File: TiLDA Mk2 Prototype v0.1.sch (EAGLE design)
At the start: 199 parts, among them IC1 ATSAM3X8EA-AU, IC10 MCP73831, IC2 MPU-6050, IC3 SRF-V1.2, IC5 S25FL216K0PMFI011, IC7 HMC5883LSMD (NP), IC8 MCP1825T-3302E/DC, IC9 TC1015-3V3, J1 ZX62-AB-5PA(11), J3 Arduino Headers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

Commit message: Parts: Miter corner board Prototype: Miter corner board
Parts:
- C101, C102, C103, C111, C133, C50: value SMC_B/10u/ -> 0805/10u/6V3/X5R
- C127, C135: value SMC_B/10u/ -> 0805/10u/6V3/X5R/(NP)
- C33, C36, C37: value 0805/22u/25V/X5R -> 0805/10u/6V3/X5R
- J6: value POWER-POD-EMF -> B016 - PowerPOD NCP1402 5V0
- J8: value (none) -> 1x02 RA Pin
- OUTLINE1: value TILDA_BOARDOUTLINE-VERYWIDE -> TILDA_BOARDOUTLINE-MITER; device TiLDA Mk2 Parts:TILDA_BOARDOUTLINE-VERYWIDE -> TiLDA Mk2 Parts:TILDA_BOARDOUTLINE-MITER
- renumbered U1 to J6
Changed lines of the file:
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@@
 <parts>
 <part name="FRAME1" library="TiLDA Mk2 Parts" deviceset="A3L-LOC" device=""/>
-<part name="OUTLINE1" library="TiLDA Mk2 Parts" deviceset="TILDA_BOARDOUTLINE" device="-VERYWIDE"/>
+<part name="OUTLINE1" library="TiLDA Mk2 Parts" deviceset="TILDA_BOARDOUTLINE" device="-MITER"/>
 <part name="LOGO1" library="TiLDA Mk2 Parts" deviceset="OSHW-LOGO" device="M"/>
 <part name="FID1" library="TiLDA Mk2 Parts" deviceset="FIDUCIAL" device="1X2.5-STOP"/>
@@
 <part name="GND17" library="TiLDA Mk2 Parts" deviceset="GND" device=""/>
 <part name="GND20" library="TiLDA Mk2 Parts" deviceset="GND" device=""/>
-<part name="C133" library="TiLDA Mk2 Parts" deviceset="CPOL-EU" device="-C0805RNDPOL" value="SMC_B/10u/"/>
+<part name="C133" library="TiLDA Mk2 Parts" deviceset="CPOL-EU" device="-C0805RNDPOL" value="0805/10u/6V3/X5R"/>
 <part name="C132" library="TiLDA Mk2 Parts" deviceset="C-EU" device="C0402-ARDUINO-ROUND" value="0402/100n/10V/X5R"/>
 <part name="GND22" library="TiLDA Mk2 Parts" deviceset="GND" device=""/>
@@
 <part name="L101" library="TiLDA Mk2 Parts" deviceset="WE-CBF" device="_0805" value="MH2029-300Y"/>
 <part name="L102" library="TiLDA Mk2 Parts" deviceset="WE-CBF" device="_0805" value="MH2029-300Y"/>
-<part name="C101" library="TiLDA Mk2 Parts" deviceset="CPOL-EU" device="-C0805RNDPOL" value="SMC_B/10u/"/>
-<part name="C111" library="TiLDA Mk2 Parts" deviceset="CPOL-EU" device="-C0805RNDPOL" value="SMC_B/10u/"/>
-<part name="C102" library="TiLDA Mk2 Parts" deviceset="CPOL-EU" device="-C0805RNDPOL" value="SMC_B/10u/"/>
-<part name="C103" library="TiLDA Mk2 Parts" deviceset="CPOL-EU" device="-C0805RNDPOL" value="SMC_B/10u/"/>
+<part name="C101" library="TiLDA Mk2 Parts" deviceset="CPOL-EU" device="-C0805RNDPOL" value="0805/10u/6V3/X5R"/>
+<part name="C111" library="TiLDA Mk2 Parts" deviceset="CPOL-EU" device="-C0805RNDPOL" value="0805/10u/6V3/X5R"/>
+<part name="C102" library="TiLDA Mk2 Parts" deviceset="CPOL-EU" device="-C0805RNDPOL" value="0805/10u/6V3/X5R"/>
+<part name="C103" library="TiLDA Mk2 Parts" deviceset="CPOL-EU" device="-C0805RNDPOL" value="0805/10u/6V3/X5R"/>
 <part name="L105" library="TiLDA Mk2 Parts" deviceset="WE-CBF" device="_0805" value="MH2029-300Y"/>
 <part name="R108" library="TiLDA Mk2 Parts" deviceset="R-EU_" device="R0402-ARDUINO-ROUND" value="0402/0R/5%/(NP)"/>
@@
 <part name="GND50" library="supply1" deviceset="GND" device=""/>
 <part name="C126" library="TiLDA Mk2 Parts" deviceset="C-EU" device="C0402-ARDUINO-ROUND" value="0402/10n/10V/Y5V"/>
-<part name="C127" library="TiLDA Mk2 Parts" deviceset="CPOL-EU" device="-C0805RNDPOL" value="SMC_B/10u/"/>
-<part name="C135" library="TiLDA Mk2 Parts" deviceset="CPOL-EU" device="-C0805RNDPOL" value="SMC_B/10u/"/>
+<part name="C127" library="TiLDA Mk2 Parts" deviceset="CPOL-EU" device="-C0805RNDPOL" value="0805/10u/6V3/X5R/(NP)"/>
+<part name="C135" library="TiLDA Mk2 Parts" deviceset="CPOL-EU" device="-C0805RNDPOL" value="0805/10u/6V3/X5R/(NP)"/>
 <part name="GND52" library="TiLDA Mk2 Parts" deviceset="GND" device=""/>
 <part name="R102" library="TiLDA Mk2 Parts" deviceset="R-EU_" device="R0402-ARDUINO-ROUND" value="0402/10K/5%"/>
 <part name="GND53" library="TiLDA Mk2 Parts" deviceset="GND" device=""/>
 <part name="R25" library="TiLDA Mk2 Parts" deviceset="R-EU_" device="R0402-ARDUINO-ROUND" value="0402/1K/5%"/>
-<part name="C36" library="TiLDA Mk2 Parts" deviceset="C-EU" device="C0805RND" value="0805/22u/25V/X5R"/>
+<part name="C36" library="TiLDA Mk2 Parts" deviceset="C-EU" device="C0805RND" value="0805/10u/6V3/X5R"/>
 <part name="C34" library="TiLDA Mk2 Parts" deviceset="C-EU" device="C0603-ROUND" value="0603/1u/10V/X5R"/>
 <part name="GND63" library="TiLDA Mk2 Parts" deviceset="GND" device=""/>
 <part name="GND64" library="TiLDA Mk2 Parts" deviceset="GND" device=""/>
-<part name="C33" library="TiLDA Mk2 Parts" deviceset="C-EU" device="C0805RND" value="0805/22u/25V/X5R"/>
+<part name="C33" library="TiLDA Mk2 Parts" deviceset="C-EU" device="C0805RND" value="0805/10u/6V3/X5R"/>
 <part name="GND65" library="TiLDA Mk2 Parts" deviceset="GND" device=""/>
 <part name="IC8" library="TiLDA Mk2 Parts" deviceset="MCP1825T-3302E/DC" device=""/>
@@
 <part name="H1" library="TiLDA Mk2 Parts" deviceset="MOUNT-HOLE" device="4.5-LWK" value=""/>
 <part name="H2" library="TiLDA Mk2 Parts" deviceset="MOUNT-HOLE" device="4.5-LWK" value=""/>
-<part name="C37" library="TiLDA Mk2 Parts" deviceset="C-EU" device="C0805RND" value="0805/22u/25V/X5R"/>
+<part name="C37" library="TiLDA Mk2 Parts" deviceset="C-EU" device="C0805RND" value="0805/10u/6V3/X5R"/>
 <part name="GND58" library="TiLDA Mk2 Parts" deviceset="GND" device=""/>
 <part name="C38" library="TiLDA Mk2 Parts" deviceset="C-EU" device="C0603-ROUND" value="0603/1u/10V/X5R"/>
@@
 <part name="R49" library="TiLDA Mk2 Parts" deviceset="R-EU_" device="R0402-ARDUINO-ROUND" value="0402/10K/5%"/>
 <part name="U2" library="TiLDA Mk2 Parts" deviceset="JHD12864-G13BSW-OUTLINE" device=""/>
-<part name="J8" library="TiLDA Mk2 Parts" deviceset="M02" device="RA"/>
+<part name="J8" library="TiLDA Mk2 Parts" deviceset="M02" device="RA" value="1x02 RA Pin"/>
 <part name="J7" library="TiLDA Mk2 Parts" deviceset="JHD12863-G13BSW-CONNECTOR" device="-SFV30R-2STE1HLF" value="SFV30R-2STE1HLF"/>
 <part name="C39" library="TiLDA Mk2 Parts" deviceset="C-EU" device="C0603-ROUND" value="0603/1u/10V/X5R"/>
@@
 <attribute name="TP_SIGNAL_NAME" value=""/>
 </part>
-<part name="U1" library="TiLDA Mk2 Parts" deviceset="POWER-POD" device="-EMF"/>
+<part name="J6" library="TiLDA Mk2 Parts" deviceset="POWER-POD" device="-EMF" value="B016 - PowerPOD NCP1402 5V0"/>
 <part name="R47" library="TiLDA Mk2 Parts" deviceset="R-EU_" device="R0402-ARDUINO-ROUND" value="0402/10K/5%"/>
 <part name="R48" library="TiLDA Mk2 Parts" deviceset="R-EU_" device="R0402-ARDUINO-ROUND" value="0402/10K/5%"/>
-<part name="C50" library="TiLDA Mk2 Parts" deviceset="CPOL-EU" device="-C0805RNDPOL" value="SMC_B/10u/"/>
+<part name="C50" library="TiLDA Mk2 Parts" deviceset="CPOL-EU" device="-C0805RNDPOL" value="0805/10u/6V3/X5R"/>
 <part name="GND9" library="TiLDA Mk2 Parts" deviceset="GND" device=""/>
 </parts>
@@
 <instance part="TP25" gate="G$1" x="673.1" y="83.82" rot="R270"/>
 <instance part="TP26" gate="G$1" x="670.56" y="182.88" rot="R270"/>
-<instance part="U1" gate="G$1" x="88.9" y="144.78"/>
+<instance part="J6" gate="G$1" x="88.9" y="144.78"/>
 <instance part="R47" gate="G$1" x="127" y="139.7" smashed="yes" rot="R90">
 <attribute name="NAME" x="128.27" y="143.7386" size="1.778" layer="95"/>
@@
 <wire x1="78.74" y1="147.32" x2="76.2" y2="147.32" width="0.1524" layer="91"/>
 <label x="76.2" y="147.32" size="1.778" layer="95" rot="MR0"/>
-<pinref part="U1" gate="G$1" pin="GND"/>
+<pinref part="J6" gate="G$1" pin="GND"/>
 </segment>
 <segment>
@@
 <wire x1="78.74" y1="149.86" x2="76.2" y2="149.86" width="0.1524" layer="91"/>
 <label x="76.2" y="149.86" size="1.778" layer="95" rot="MR0"/>
-<pinref part="U1" gate="G$1" pin="VIN"/>
+<pinref part="J6" gate="G$1" pin="VIN"/>
 </segment>
 <segment>
@@
 <wire x1="78.74" y1="144.78" x2="76.2" y2="144.78" width="0.1524" layer="91"/>
 <label x="76.2" y="144.78" size="1.778" layer="95" rot="MR0"/>
-<pinref part="U1" gate="G$1" pin="VOUT"/>
-</segment>
-</net>
+<pinref part="J6" gate="G$1" pin="VOUT"/>
+</segment>
+</net>

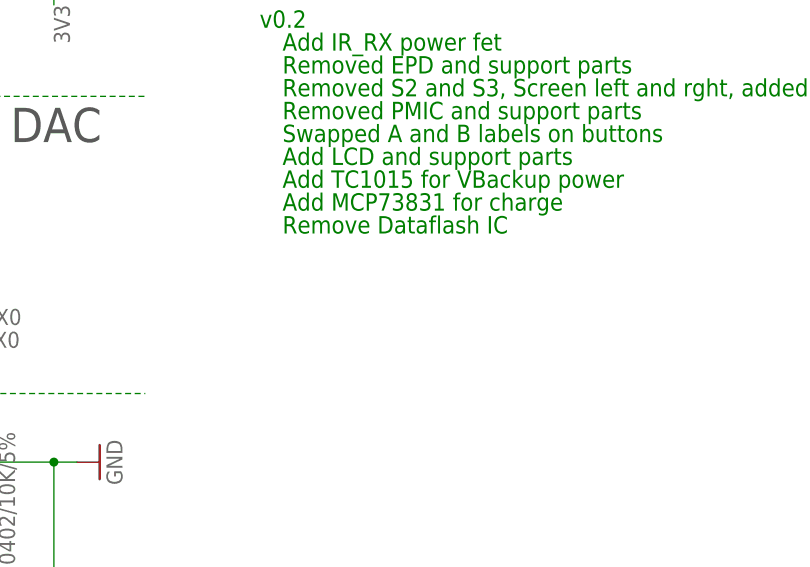
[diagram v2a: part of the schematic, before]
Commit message: Prototype: Slik screen updates
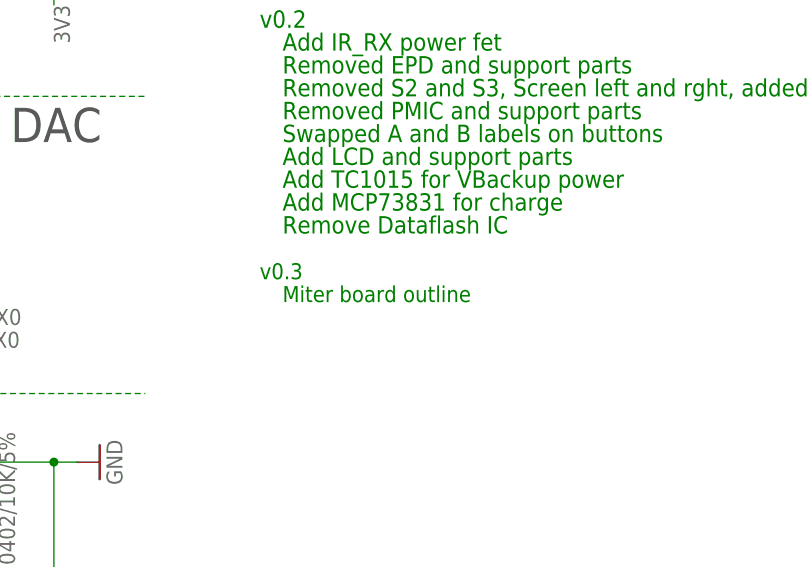
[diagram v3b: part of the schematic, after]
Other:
- note added: "Miter board outline"
- note added: "v0.3"
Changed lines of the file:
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@@
 <text x="474.98" y="2.54" size="1.9304" layer="91" rot="R90">VDDIO</text>
 <text x="487.68" y="2.54" size="1.9304" layer="91" rot="R90">VDDIO</text>
+<text x="795.02" y="147.32" size="1.778" layer="91">v0.3</text>
+<text x="797.56" y="144.78" size="1.778" layer="91">Miter board outline</text>
 </plain>
 <instances>

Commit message: Prototype: fixed LCD conections
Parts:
- Q12: value BSS84W -> 2N7002KW; device TiLDA Mk2 Parts:MOSFET-P-SC70-3 -> TiLDA Mk2 Parts:MOSFET-NSC70-3
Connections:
- removed net LCD_A: R45.1, U2.A
- new net N$1: R45.1, U2.K
- net 3V3: now also U2.A; no longer Q12.S, R43.2
- net GND: now also Q12.S, R43.2; no longer U2.K
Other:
- moved on the sheet: R45
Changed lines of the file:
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@@
 <attribute name="TP_SIGNAL_NAME" value=""/>
 </part>
-<part name="Q12" library="TiLDA Mk2 Parts" deviceset="MOSFET-P" device="-SC70-3" value="BSS84W"/>
 <part name="TP22" library="TiLDA Mk2 Parts" deviceset="TP" device="B1,27" value="PC12">
 <attribute name="TP_SIGNAL_NAME" value=""/>
@@
 <part name="C50" library="TiLDA Mk2 Parts" deviceset="CPOL-EU" device="-C0805RNDPOL" value="0805/10u/6V3/X5R"/>
 <part name="GND9" library="TiLDA Mk2 Parts" deviceset="GND" device=""/>
+<part name="Q12" library="TiLDA Mk2 Parts" deviceset="MOSFET-N" device="SC70-3" value="2N7002KW"/>
 </parts>
 <sheets>
@@
 <instance part="C46" gate="G$1" x="342.9" y="172.72" rot="R180"/>
 <instance part="C47" gate="G$1" x="347.98" y="172.72" rot="R180"/>
-<instance part="R45" gate="G$1" x="38.1" y="218.44"/>
+<instance part="R45" gate="G$1" x="40.64" y="218.44"/>
 <instance part="Q11" gate="G$1" x="264.16" y="162.56"/>
 <instance part="R43" gate="G$1" x="71.12" y="226.06"/>
@@
 </instance>
 <instance part="R46" gate="G$1" x="76.2" y="93.98" rot="R270"/>
-<instance part="GND1" gate="1" x="33.02" y="228.6" rot="R90"/>
+<instance part="GND1" gate="1" x="88.9" y="213.36"/>
 <instance part="GND2" gate="1" x="297.18" y="208.28" rot="R270"/>
 <instance part="GND3" gate="1" x="355.6" y="170.18"/>
@@
 <instance part="TP20" gate="G$1" x="683.26" y="172.72" rot="R270"/>
 <instance part="TP21" gate="G$1" x="673.1" y="119.38" rot="R270"/>
-<instance part="Q12" gate="G$1" x="60.96" y="218.44" rot="R270"/>
 <instance part="TP22" gate="G$1" x="675.64" y="106.68" rot="R270"/>
 <instance part="TP24" gate="G$1" x="584.2" y="40.64" rot="R180"/>
@@
 </instance>
 <instance part="GND9" gate="1" x="91.44" y="38.1"/>
+<instance part="Q12" gate="G$1" x="60.96" y="220.98" rot="MR270"/>
 </instances>
 <busses>
@@
 </segment>
 <segment>
-<pinref part="U2" gate="OUTLINE" pin="K"/>
-<wire x1="27.94" y1="228.6" x2="30.48" y2="228.6" width="0.1524" layer="91"/>
-<pinref part="GND1" gate="1" pin="GND"/>
-</segment>
-<segment>
 <pinref part="C50" gate="G$1" pin="-"/>
 <pinref part="GND9" gate="1" pin="GND"/>
 <wire x1="91.44" y1="40.64" x2="91.44" y2="43.18" width="0.1524" layer="91"/>
 </segment>
+<segment>
+<wire x1="88.9" y1="215.9" x2="88.9" y2="218.44" width="0.1524" layer="91"/>
+<pinref part="R43" gate="G$1" pin="2"/>
+<wire x1="88.9" y1="218.44" x2="66.04" y2="218.44" width="0.1524" layer="91"/>
+<wire x1="76.2" y1="226.06" x2="88.9" y2="226.06" width="0.1524" layer="91"/>
+<wire x1="88.9" y1="226.06" x2="88.9" y2="218.44" width="0.1524" layer="91"/>
+<junction x="88.9" y="218.44"/>
+<pinref part="GND1" gate="1" pin="GND"/>
+<pinref part="Q12" gate="G$1" pin="S"/>
+</segment>
 </net>
 <net name="PD10" class="0">
@@
 </segment>
 <segment>
-<wire x1="91.44" y1="218.44" x2="88.9" y2="218.44" width="0.1524" layer="91"/>
-<label x="91.44" y="218.44" size="1.778" layer="95"/>
-<pinref part="Q12" gate="G$1" pin="S"/>
-<pinref part="R43" gate="G$1" pin="2"/>
-<wire x1="88.9" y1="218.44" x2="66.04" y2="218.44" width="0.1524" layer="91"/>
-<wire x1="76.2" y1="226.06" x2="88.9" y2="226.06" width="0.1524" layer="91"/>
-<wire x1="88.9" y1="226.06" x2="88.9" y2="218.44" width="0.1524" layer="91"/>
-<junction x="88.9" y="218.44"/>
-</segment>
-<segment>
 <pinref part="Q11" gate="G$1" pin="S"/>
 <wire x1="264.16" y1="190.5" x2="264.16" y2="187.96" width="0.1524" layer="91"/>
@@
 <label x="561.34" y="226.06" size="1.9304" layer="95" rot="MR90"/>
 </segment>
+<segment>
+<pinref part="U2" gate="OUTLINE" pin="A"/>
+<wire x1="30.48" y1="228.6" x2="27.94" y2="228.6" width="0.1524" layer="91"/>
+<label x="30.48" y="228.6" size="1.778" layer="95"/>
+</segment>
 </net>
 <net name="LCD_POWER" class="0">
@@
 <label x="63.5" y="228.6" size="1.778" layer="95" rot="R90"/>
 <wire x1="63.5" y1="223.52" x2="63.5" y2="226.06" width="0.1524" layer="91"/>
-<pinref part="Q12" gate="G$1" pin="G"/>
 <pinref part="R43" gate="G$1" pin="1"/>
 <wire x1="63.5" y1="226.06" x2="63.5" y2="228.6" width="0.1524" layer="91"/>
 <wire x1="66.04" y1="226.06" x2="63.5" y2="226.06" width="0.1524" layer="91"/>
 <junction x="63.5" y="226.06"/>
+<pinref part="Q12" gate="G$1" pin="G"/>
 </segment>
 <segment>
@@
 </segment>
 </net>
-<net name="LCD_A" class="0">
-<segment>
-<pinref part="R45" gate="G$1" pin="1"/>
-<pinref part="U2" gate="OUTLINE" pin="A"/>
-<wire x1="33.02" y1="218.44" x2="27.94" y2="218.44" width="0.1524" layer="91"/>
-</segment>
-</net>
 <net name="LCD_V1" class="0">
 <segment>
@@
 <segment>
 <pinref part="R45" gate="G$1" pin="2"/>
+<wire x1="55.88" y1="218.44" x2="45.72" y2="218.44" width="0.1524" layer="91"/>
 <pinref part="Q12" gate="G$1" pin="D"/>
-<wire x1="55.88" y1="218.44" x2="43.18" y2="218.44" width="0.1524" layer="91"/>
 </segment>
 </net>
@@
 </segment>
 </net>
+<net name="N$1" class="0">
+<segment>
+<pinref part="U2" gate="OUTLINE" pin="K"/>
+<pinref part="R45" gate="G$1" pin="1"/>
+<wire x1="27.94" y1="218.44" x2="35.56" y2="218.44" width="0.1524" layer="91"/>
+</segment>
+</net>

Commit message: Prototype: more curves
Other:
- note added: "Off"
- note added: "On"
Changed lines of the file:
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@@
 <text x="795.02" y="147.32" size="1.778" layer="91">v0.3</text>
 <text x="797.56" y="144.78" size="1.778" layer="91">Miter board outline</text>
+<text x="88.9" y="7.62" size="1.778" layer="91">On</text>
+<text x="88.9" y="17.78" size="1.778" layer="91">Off</text>
 </plain>
 <instances>

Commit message: Prototype: Allow power from just USB
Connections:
- removed net 4V2: S8.O
- net VBUS: now also S8.O
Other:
- note added: "Allow power from USB"
- note added: "Battery is charged in both cases"
- note added: "Curve all the tracks"
- note added: "Off posotion power is taken from USB"
- note added: "Off/USB"
- note added: "On posotion power is taken from the battery"
- note added: "On/Battery"
- note added: "Silk screen updates"
- note added: "v0.333333333333333333"
- note removed: "Off"
- note removed: "On"
- note removed: "v0.3"
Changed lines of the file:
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@@
 <text x="474.98" y="2.54" size="1.9304" layer="91" rot="R90">VDDIO</text>
 <text x="487.68" y="2.54" size="1.9304" layer="91" rot="R90">VDDIO</text>
-<text x="795.02" y="147.32" size="1.778" layer="91">v0.3</text>
+<text x="795.02" y="147.32" size="1.778" layer="91">v0.333333333333333333</text>
 <text x="797.56" y="144.78" size="1.778" layer="91">Miter board outline</text>
-<text x="88.9" y="7.62" size="1.778" layer="91">On</text>
-<text x="88.9" y="17.78" size="1.778" layer="91">Off</text>
+<text x="73.66" y="7.62" size="1.778" layer="91">On/Battery</text>
+<text x="73.66" y="17.78" size="1.778" layer="91">Off/USB</text>
+<text x="797.56" y="142.24" size="1.778" layer="91">Silk screen updates </text>
+<text x="797.56" y="139.7" size="1.778" layer="91">Curve all the tracks</text>
+<text x="797.56" y="137.16" size="1.778" layer="91">Allow power from USB</text>
+<text x="800.1" y="134.62" size="1.778" layer="91">On posotion power is taken from the battery</text>
+<text x="800.1" y="132.08" size="1.778" layer="91">Off posotion power is taken from USB</text>
+<text x="800.1" y="129.54" size="1.778" layer="91">Battery is charged in both cases</text>
 </plain>
 <instances>
@@
 <junction x="43.18" y="104.14"/>
 </segment>
+<segment>
+<pinref part="S8" gate="1" pin="O"/>
+<wire x1="109.22" y1="15.24" x2="101.6" y2="15.24" width="0.1524" layer="91"/>
+<label x="109.22" y="15.24" size="1.778" layer="95"/>
+</segment>
 </net>
 <net name="JTAG_RESET" class="0">
@@
 </segment>
 </net>
-<net name="4V2" class="0">
-<segment>
-<pinref part="S8" gate="1" pin="O"/>
-<wire x1="109.22" y1="15.24" x2="101.6" y2="15.24" width="0.1524" layer="91"/>
-<label x="109.22" y="15.24" size="1.778" layer="95"/>
-</segment>
-</net>
